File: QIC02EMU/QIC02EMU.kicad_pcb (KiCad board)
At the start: 2 copper layers, 95.2 x 76.2 mm, 23 parts, among them J1 2.5 mm Barrel DC JACK, J2 Micro_SD_Card_Det, J3 50 Pin header, J4 DB37_F, U1 STM32BluePill, U2 74ABT657, U3 74ABT241

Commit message: Fixed a problem with the direction and one enable of the 241.
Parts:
- turned C4 to 180 degrees
- turned U2 to 180 degrees
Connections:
- U1 pad 27: Net-(U1-Pad27) -> /TR_EN
- U2 pad 1: /IDIR -> /TR_EN
- U2 pad 10: /~HB7 -> /D0
- U2 pad 14: /D7 -> /~HB0
- U2 pad 15: /D6 -> /~HB1
- U2 pad 16: /D5 -> /~HB2
- U2 pad 17: /D4 -> /~HB3
- U2 pad 2: /~HB0 -> /D7
- U2 pad 20: /D3 -> /~HB4
- U2 pad 21: /D2 -> /~HB5
- U2 pad 22: /D1 -> /~HB6
- U2 pad 23: /D0 -> /~HB7
- U2 pad 3: /~HB1 -> /D6
- U2 pad 4: /~HB2 -> /D5
- U2 pad 5: /~HB3 -> /D4
- U2 pad 6: /~HB4 -> /D3
- U2 pad 8: /~HB5 -> /D2
- U2 pad 9: /~HB6 -> /D1
- U3 pad 19: GND -> +5V
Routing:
- net /PE: track 40.8 -> 7.00 mm, vias 3 -> 0
- net /TR_EN: track 0.00 -> 31.7 mm
- net /IDIR: track 33.3 -> 7.33 mm
- net /~HBP: track 75.3 -> 59.3 mm
- net +5V: track 98.1 -> 102.5 mm, vias 2 -> 4
- net GND: track 288.7 -> 286.4 mm, vias 6 -> 2
- net /~HB4: track 35.7 -> 36.7 mm
- net /D1: track 6.56 -> 6.04 mm
- net /~HB7: track 36.5 -> 35.9 mm
- net /~HB5: track 35.6 -> 36.1 mm
- net /D0: track 6.04 -> 5.51 mm
- net /D2: track 47.9 -> 48.4 mm
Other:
- board text added: "1"

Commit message: Update with inverter.
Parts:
- added R7: 68k, Resistor_SMD:R_0805_2012Metric, F.Cu at (119.4, 93.0)
- added U4: 74LVC1G04, Package_TO_SOT_SMD:SOT-23-5, F.Cu at (119.5, 96.5)
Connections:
- U1 pad 27: /TR_EN -> Net-(U1-Pad27)
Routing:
- net /IDIR: track 7.33 -> 24.0 mm
- net /TR_EN: track 31.7 -> 47.9 mm
- net +5V: track 102.5 -> 111.6 mm
- net GND: track 286.4 -> 281.8 mm

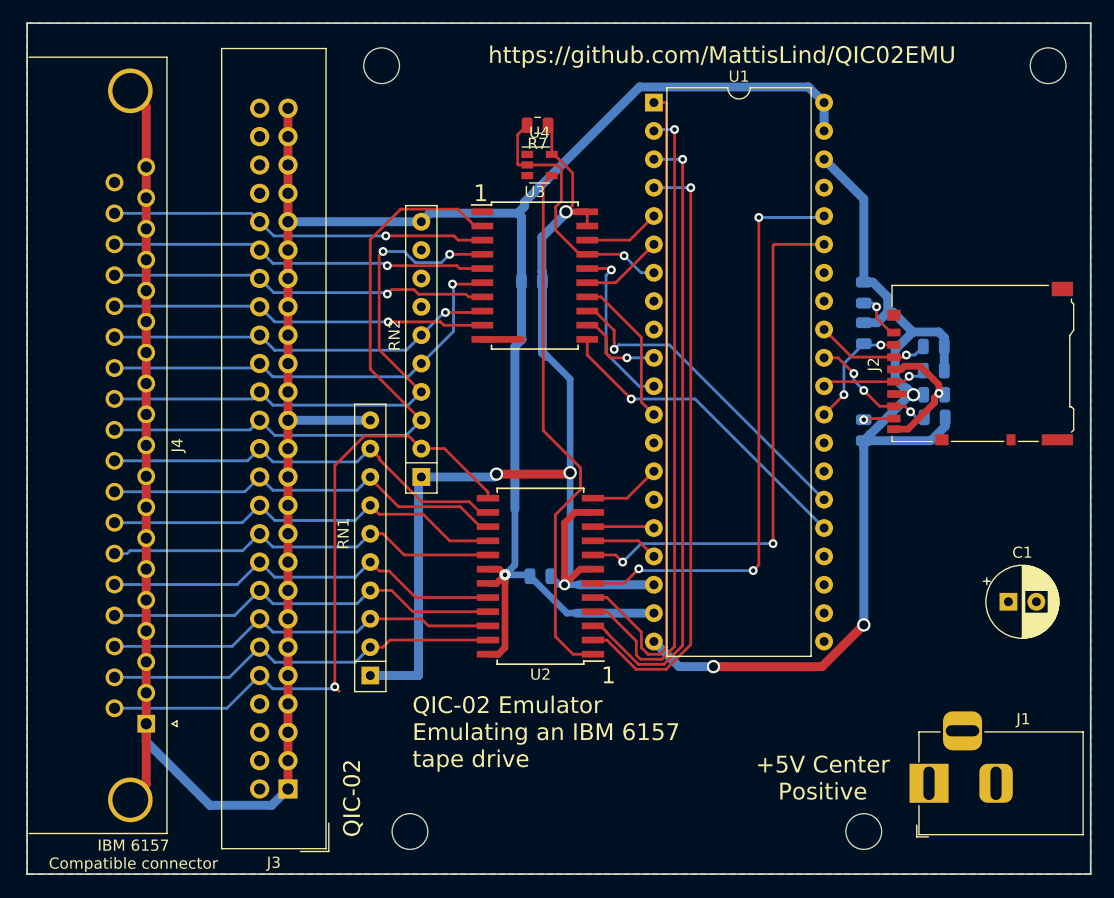
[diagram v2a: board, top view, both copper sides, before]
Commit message: Fixed VDD/VSS issue on SD card.
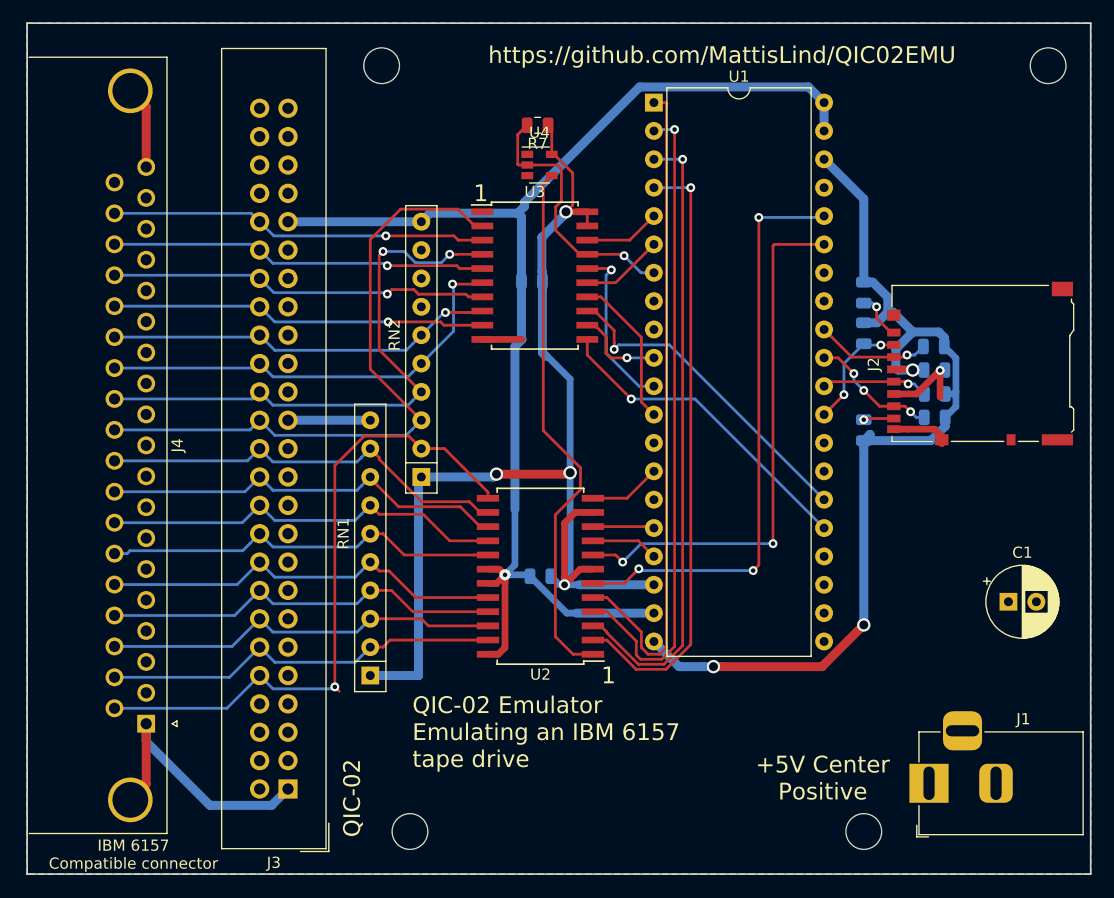
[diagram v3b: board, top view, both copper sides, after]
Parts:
- moved C3 2.21 mm to (154.9, 114.9)
- moved R3 2.10 mm to (155.0, 117.0)
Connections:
- J2 pad 4: GND -> +3V3
- J2 pad 6: +3V3 -> GND
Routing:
- net GND: track 281.8 -> 172.3 mm
- net +3V3: track 90.3 -> 89.6 mm
